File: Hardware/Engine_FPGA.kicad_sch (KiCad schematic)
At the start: 7 parts, among them J11 JTAG

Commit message: Routed the VDP-board further, as well as making it a 4-layer board - also added an exception in the gitignore, for big images.
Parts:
- added SW1: SW_DIP_x03, Button_Switch_SMD:SW_DIP_SPSTx03_Slide_6.7x9.18mm_W8.61mm_P2.54mm_LowProfile, symbol Switch:SW_DIP_x03
- U2: value (none) -> AT40K20-2EQJ; footprint (none) -> Package_QFP:PQFP-240_32.1x32.1mm_P0.5mm
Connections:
- net CCLK: now also SW1.3; no longer J11.9 (Pin_9)
- net ~{CHECK}: now also J11.7 (Pin_7); no longer J11.5 (Pin_5)
- net ~{CON}: now also J11.9 (Pin_9); no longer J11.7 (Pin_7)
- net ~{RESET}: now also SW1.1; no longer J11.1 (Pin_1)
- net ~{WAIT}: now also U2.56 (IO47/OTS)
- net TSTCLK: now reaches U2.181 (TSTCLK)
- net TSTCLK: now also J11.4 (Pin_4)
- net AUX+: now reaches U2.228 (IO181)
- net AUX-: now reaches U2.229 (IO182)
- net ENG_~{INT}/INIT renamed ENG_~{INT}
- net ENG_~{INT}: now also SW1.2
- net ~{INT}/INIT renamed INIT
- net INIT: now also SW1.5
- new net CI: J11.5 (Pin_5), SW1.4
- new net DO: J11.1 (Pin_1), SW1.6
- no-connect marks 5 -> 2
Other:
- note added: "switch-examples: ---- KJ06RTT = 6,2 x 15,24 mm (6pos) 219-6LPSTR = 7,62 x 16,71 mm (6pos) DS04-254-2-05BK-SMT = 6,2 x 16,24 mm (5 pos)"
- moved on the sheet: J11, U2A, U2B, U2C, U2E, U2F, U2G

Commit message: Finished the VDP-board, finished up the mixer-section, removed the buffer-pins from the FPGA, and instead added external buffers for the slots, designed a marquee-block with the Ultra-MSX logo, designed the logotype, andmultiple other changes.
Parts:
- renumbered J11 to J12
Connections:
- net B_CLK is gone; now on net ~{M1}: U2.111 (IO89)
- net ~{B_M1} is gone; now on net SMDAT3: U2.110 (IO88)
- net ~{B_RD} is gone; now on net SMDAT1: U2.108 (IO86)
- net ~{B_WR} is gone; now on net SMDAT2: U2.109 (IO87)
- net SMDAT1: no longer U2.104 (IO83)
- net SMDAT2: no longer U2.105 (IO84)
- net SMDAT3: no longer U2.107 (IO85)
- net BA0: no longer names the net of U2.64 (IO50/HDC)
- net BA1: no longer names the net of U2.65 (IO51)
- net BA10: no longer names the net of U2.74 (IO60)
- net BA11: no longer names the net of U2.76 (IO61)
- net BA12: no longer names the net of U2.77 (IO62)
- net BA13: no longer names the net of U2.78 (IO63)
- net BA14: no longer names the net of U2.79 (IO64)
- net BA15: no longer names the net of U2.81 (IO65)
- net BA2: no longer names the net of U2.66 (IO52)
- net BA3: no longer names the net of U2.67 (IO53)
- net BA4: no longer names the net of U2.68 (IO54/LDC)
- net BA5: no longer names the net of U2.69 (IO55)
- net BA6: no longer names the net of U2.70 (IO56)
- net BA7: no longer names the net of U2.71 (IO57)
- net BA8: no longer names the net of U2.72 (IO58)
- net BA9: no longer names the net of U2.73 (IO59)
- net BD0: no longer names the net of U2.82 (IO66)
- net BD1: no longer names the net of U2.84 (IO67)
- net BD2: no longer names the net of U2.85 (IO68)
- net BD3: no longer names the net of U2.86 (IO69)
- net BD4: no longer names the net of U2.87 (IO70)
- net BD5: no longer names the net of U2.94 (IO75)
- net BD6 renamed I2C_~{WP}
- net BD7 renamed I2C_AD1
- net ~{B_IORQ} renamed I2C_AD2
- net ~{B_MREQ} renamed I2C_SCL
- net ~{B_RESET} renamed I2C_AD3
- net ~{B_RFSH} renamed ~{RFSH}
- new net I2C_SDA: U2.104 (IO83)
- new net SLT_DIR: U2.105 (IO84)
- new net ~{MREQ}: U2.107 (IO85)
- no-connect marks 2 -> 24
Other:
- note added: "DO (data out) CHECK CON INIT/ERR CI (clock in) CO (clock out) VCC (VTref) GND N/C ATDH40M AT40KEL-DK"
- note added: "I^{2}C Signals"
- note added: "Sample Rom"
- note added: "USB & Display Port"
- note added: "Voltage-converters"
- note removed: "(for MSX expansion slots)"
- note removed: "Addressing"
- note removed: "BUFFERED SIGNALS"
- note removed: "D0 (data out) CHECK CON INIT/ERR CI (clock in) CO (clock out) VCC (VTref) GND N/C ATDH40M AT40KEL-DK"
- note removed: "Data"
- note removed: "Get a combined converter-chip, that can do both JTAG and SPI to GPIO?"
- note removed: "USB + Display Port"
- moved on the sheet: J12, R73, R74, R75, R76, R77, SW1

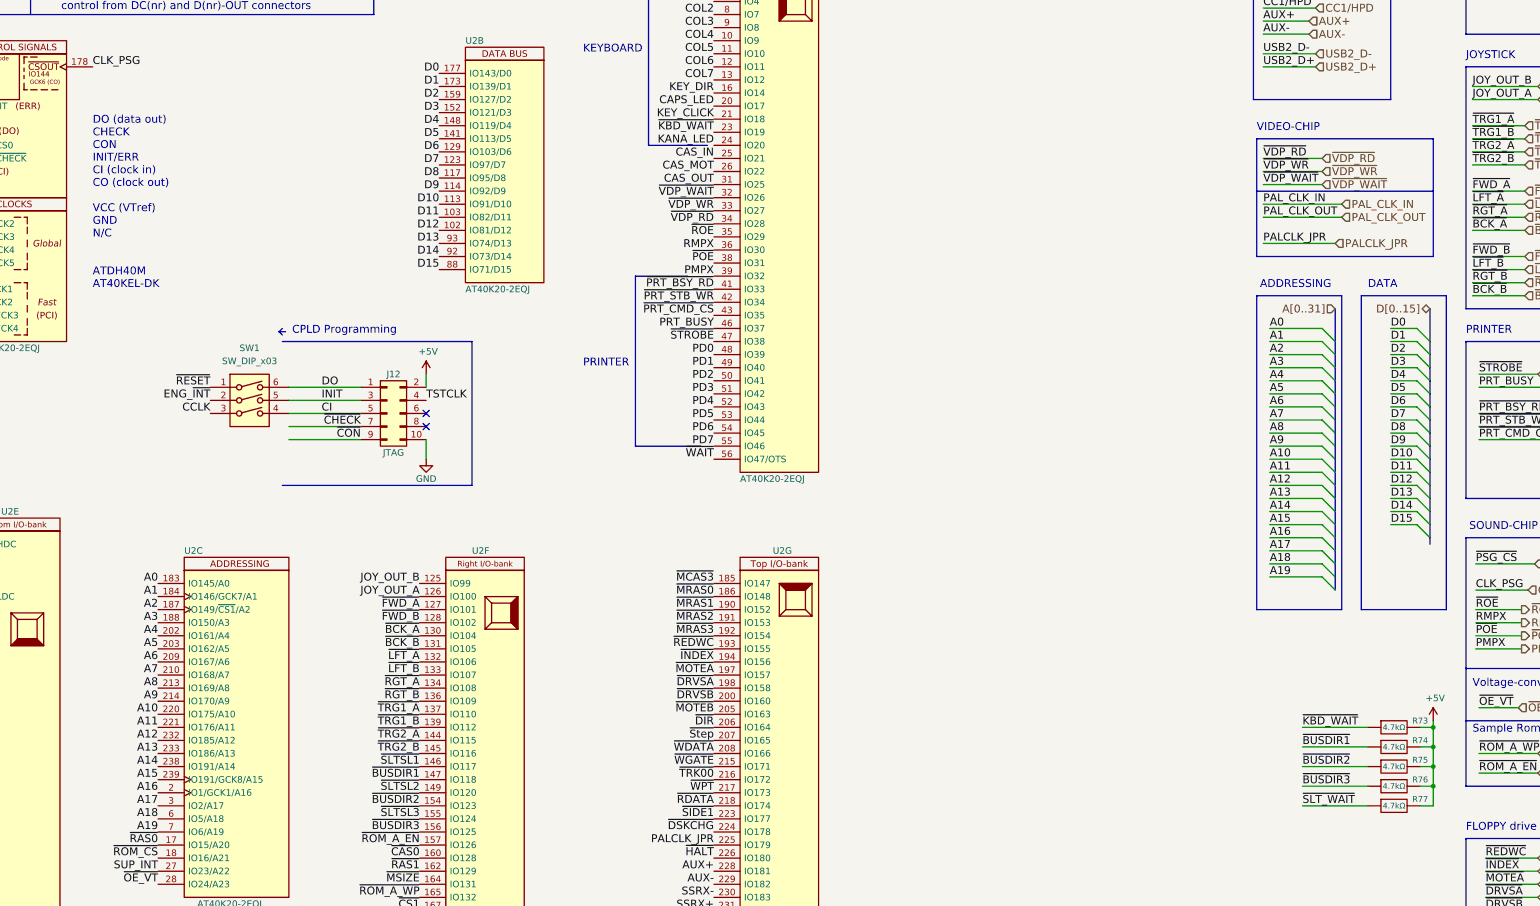
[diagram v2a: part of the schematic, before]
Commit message: Started routing the Cassette-player on the PCB.
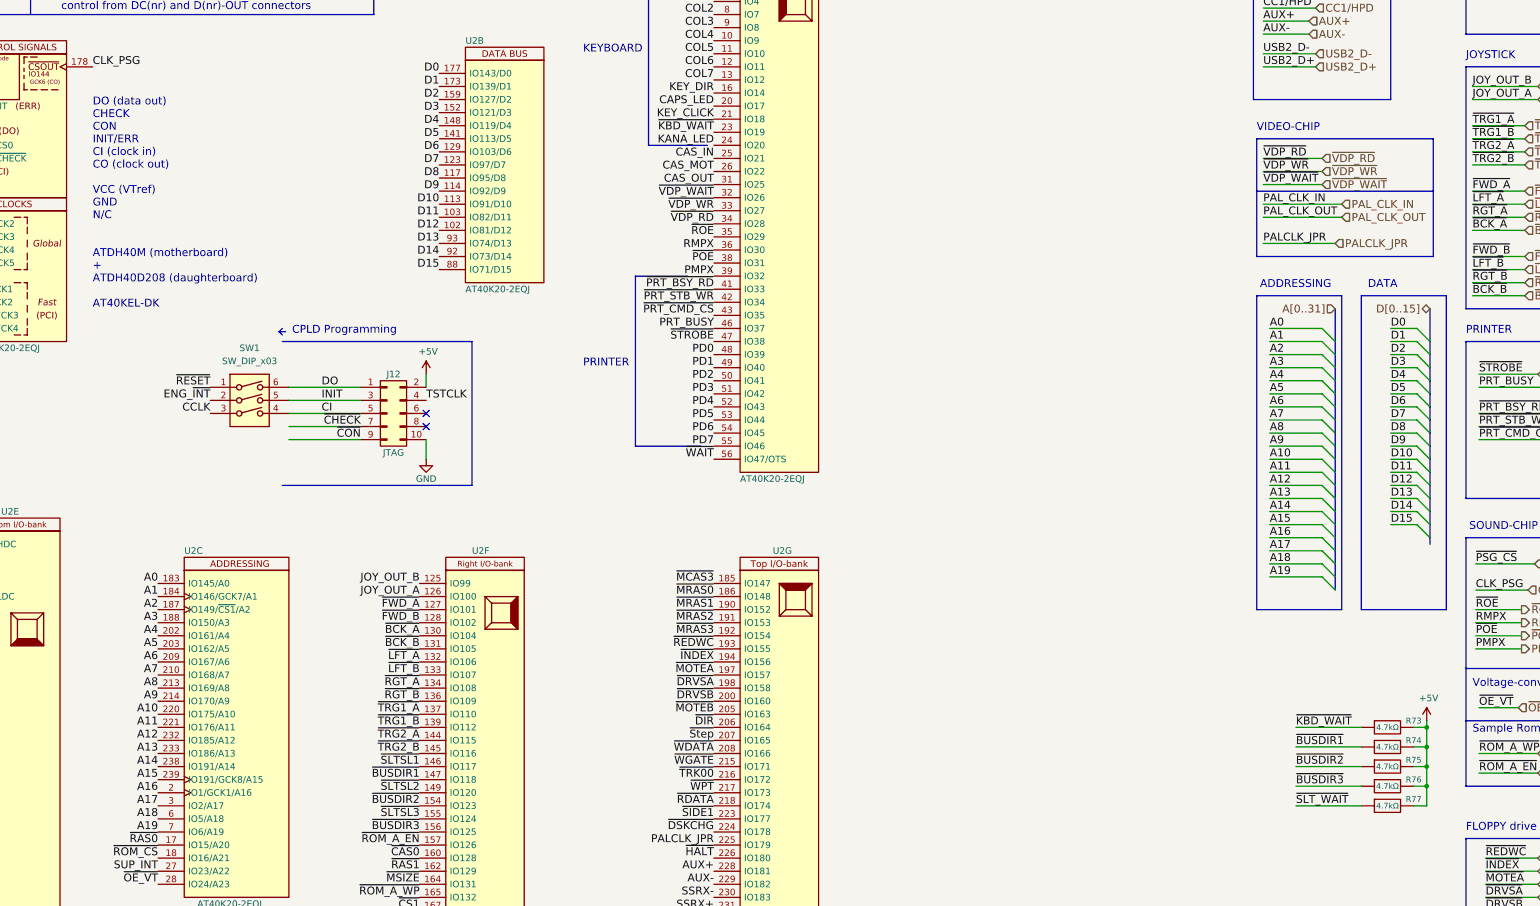
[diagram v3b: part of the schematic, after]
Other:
- note added: "DO (data out) CHECK CON INIT/ERR CI (clock in) CO (clock out) VCC (VTref) GND N/C ATDH40M (motherboard) + ATDH40D208 (daughterboard) AT40KEL-DK"
- note removed: "DO (data out) CHECK CON INIT/ERR CI (clock in) CO (clock out) VCC (VTref) GND N/C ATDH40M AT40KEL-DK"
- moved on the sheet: R73, R74, R75, R76, R77

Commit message: Added SD-card slot, made basic 3d-model for sd-card slot, connected it up in the schematic, and numerous other tweaks.
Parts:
- removed SW1: SW_DIP_x03, Button_Switch_SMD:SW_DIP_SPSTx03_Slide_6.7x9.18mm_W8.61mm_P2.54mm_LowProfile, symbol Switch:SW_DIP_x03
- added SW1: SW_KJ06RTT, LRJ:SW_DIP_DPSTx06_Slide_CIT_KJ06RTT_W6.2mm_P2.54mm, symbol LRJ-parts:SW_KJ06RTT
- J12: value JTAG -> Conn_02x05_Odd_Even
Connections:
- net +5V: no longer J12.2 (Pin_2)
- net CCLK: now also SW1.3
- net CI: now also SW1.9
- net DO: now also SW1.7
- net ENG_~{INT}: now also SW1.2
- net ENG_~{M0}: now also SW1.4
- net ENG_~{M1}: now also SW1.5
- net ENG_~{M2}: now also SW1.6
- net GND: now also SW1.10, SW1.11, SW1.12; no longer J12.10 (Pin_10)
- net INIT: now also SW1.8
- net SUP_INT: now also U2.28 (IO24/A23); no longer U2.27 (IO23/A22)
- net ~{OE_VT}: now also U2.27 (IO23/A22); no longer U2.28 (IO24/A23)
- net ~{RESET}: now also SW1.1
- net SD_MOSI/DAT2: now reaches U2.79 (IO64)
- net SD_DAT3: now reaches U2.81 (IO65)
- net SD_CMD: now reaches U2.82 (IO66)
- net SD_CLK: now reaches U2.84 (IO67)
- net SD_MISO/DAT0: now reaches U2.85 (IO68)
- net SD_DAT1: now reaches U2.86 (IO69)
- net SD_DET_A: now reaches U2.87 (IO70)
- net SD_DET_B: now reaches U2.94 (IO75)
- net I2C_~{WP} renamed I2C_AD4
- new net +5VP: J12.2 (Pin_2)
- new net GND2: J12.10 (Pin_10)
- no-connect marks 24 -> 16
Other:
- note added: "System Control"
- moved on the sheet: J12, R73, R74, R75, R76, R77, U2B, U2C, U2F, U2G

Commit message: Redesigned VDP-board to include a socket, increased it to 4 layers. Various clean-ups here and there. Improved the printer-port and joystick-port 3D-models. Improved the cooling-fin 3D-model, and added attachment-spring in 3D-model.
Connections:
- net ~{M1_Z80}: now reaches U2.64 (IO50/HDC)
- net ~{MREQ_Z80}: now reaches U2.65 (IO51)
- net ~{IORQ_Z80}: now reaches U2.66 (IO52)
- net Z80_D0: now reaches U2.67 (IO53)
- net Z80_D1: now reaches U2.68 (IO54/LDC)
- net Z80_D2: now reaches U2.69 (IO55)
- net Z80_D3: now reaches U2.70 (IO56)
- net Z80_D4: now reaches U2.71 (IO57)
- net Z80_D5: now reaches U2.72 (IO58)
- net Z80_D6: now reaches U2.73 (IO59)
- net Z80_D7: now reaches U2.74 (IO60)
- net ~{SLT_RST}: now reaches U2.76 (IO61)
- net ~{VDP_RST}: now reaches U2.77 (IO62)
- net ~{AUD_RST}: now reaches U2.78 (IO63)
- net PALCLK_JPR renamed NTSC_CLKO
- no-connect marks 16 -> 2
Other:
- note added: "Micro-SD card"
- note added: "Z80 inside of MSX-Engine"
- moved on the sheet: J12, R73, R74, R75, R76, R77, SW1, U2A, U2B, U2D, U2E

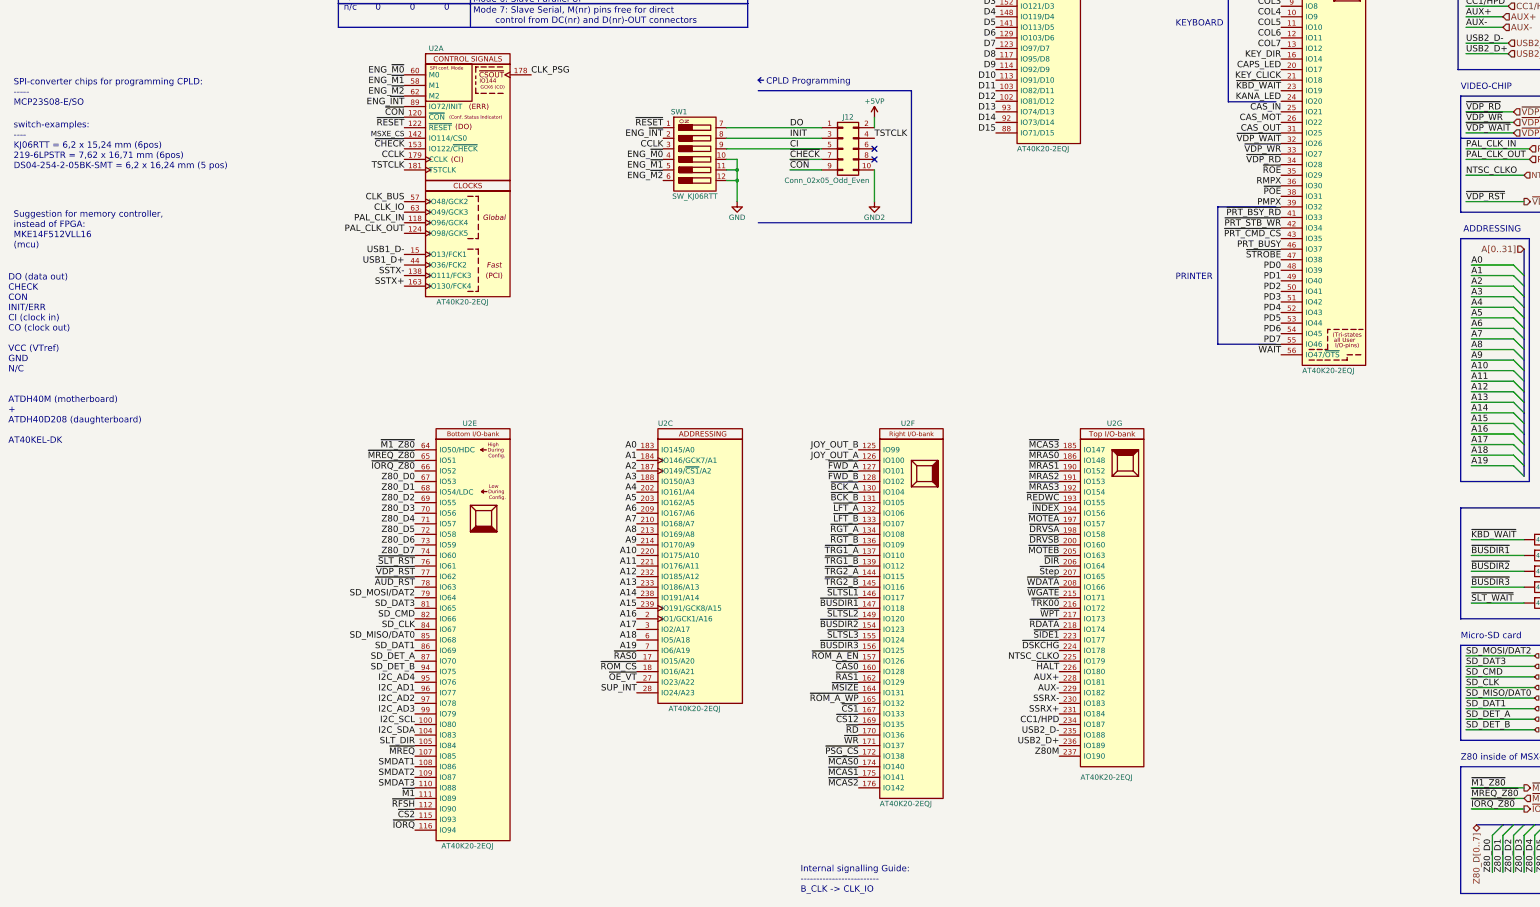
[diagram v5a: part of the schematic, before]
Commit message: Generated first PDF-files
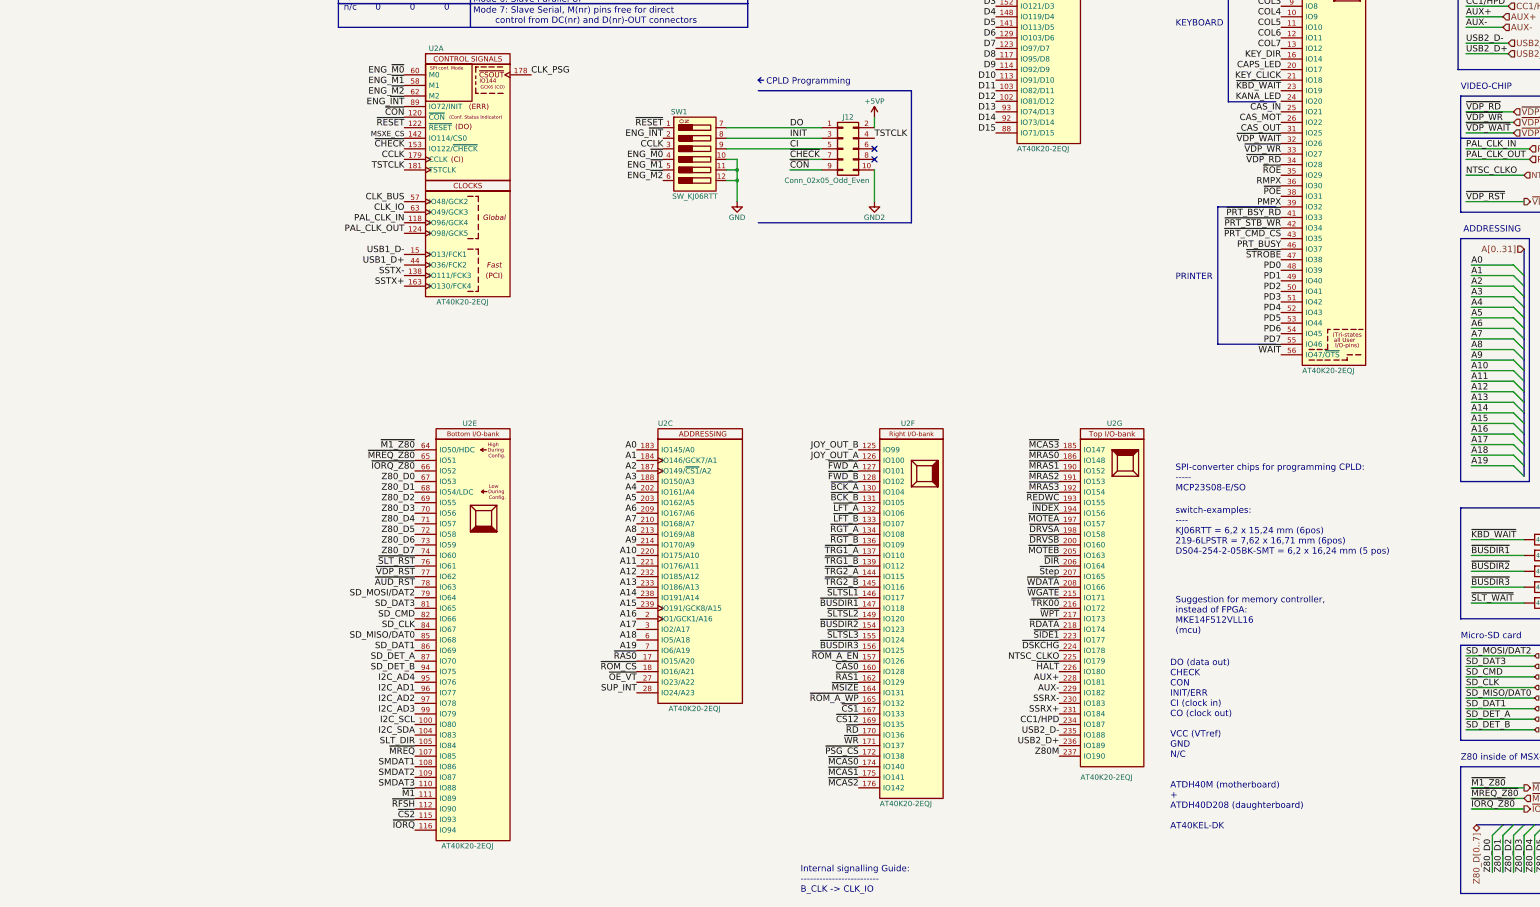
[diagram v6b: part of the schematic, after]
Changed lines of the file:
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@@
   )
   (text "Suggestion for memory controller,\ninstead of FPGA:\nMKE14F512VLL16\n(mcu)"
-    (at -60.96 101.6 0)
+    (at 218.44 194.31 0)
     (effects (font (size 1.524 1.524)) (justify left bottom))
   )
@@
   )
   (text "switch-examples:\n----\nKJ06RTT = 6,2 x 15,24 mm (6pos)\n219-6LPSTR = 7,62 x 16,71 mm (6pos)\nDS04-254-2-05BK-SMT = 6,2 x 16,24 mm (5 pos)"
-    (at -60.96 82.55 0)
+    (at 218.44 175.26 0)
     (effects (font (size 1.524 1.524)) (justify left bottom))
   )
@@
   )
   (text "DO (data out)\nCHECK\nCON\nINIT/ERR\nCI (clock in)\nCO (clock out)\n\nVCC (VTref)\nGND\nN/C\n\n\nATDH40M (motherboard)\n+ \nATDH40D208 (daughterboard)\n\nAT40KEL-DK\n"
-    (at -62.23 148.59 0)
+    (at 217.17 241.3 0)
     (effects (font (size 1.524 1.524)) (justify left bottom))
   )
@@
   )
   (text "SPI-converter chips for programming CPLD:\n-----\nMCP23S08-E/SO"
-    (at -60.96 67.31 0)
+    (at 218.44 160.02 0)
     (effects (font (size 1.524 1.524)) (justify left bottom))
   )
